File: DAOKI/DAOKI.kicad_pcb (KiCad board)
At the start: 2 copper layers, 34 x 14 mm, 15 parts, among them CON4 CON4, U1 MOCH22a1, U2 LM393

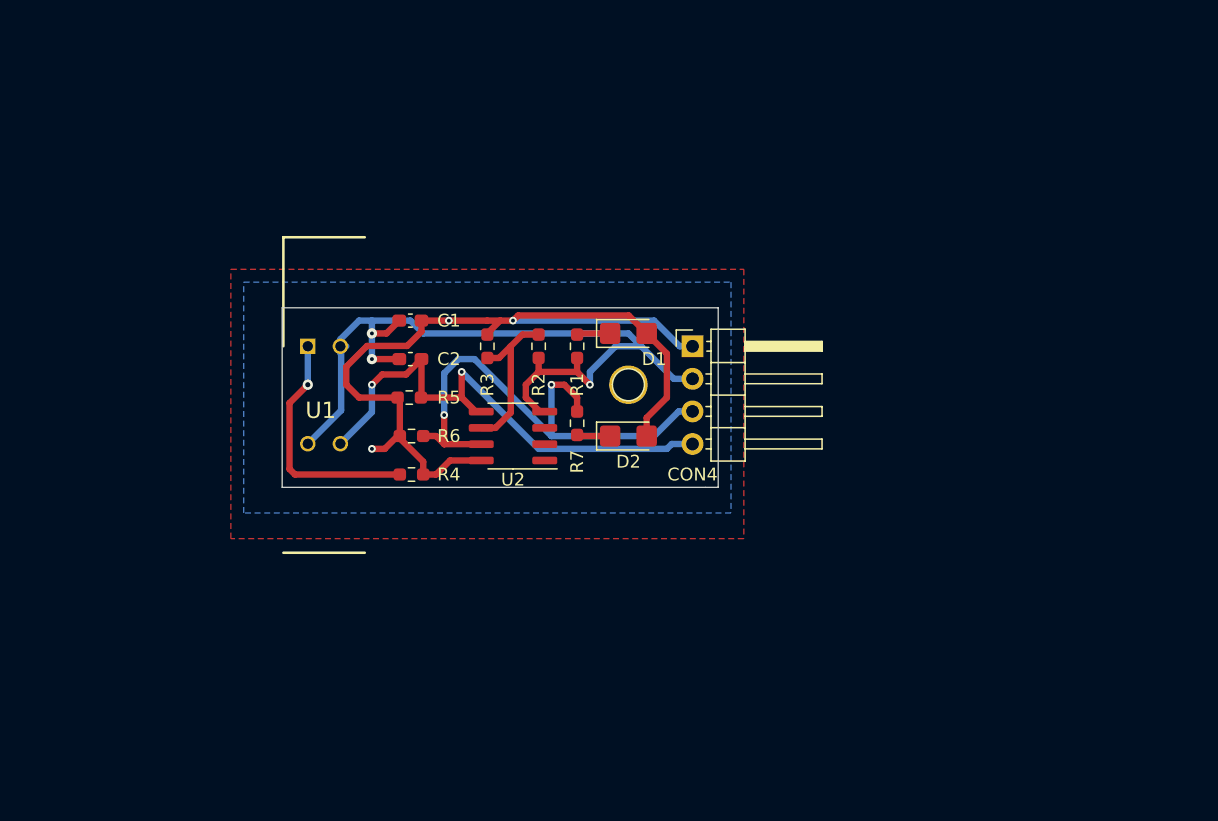
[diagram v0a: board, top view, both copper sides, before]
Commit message: Some schematic improvements
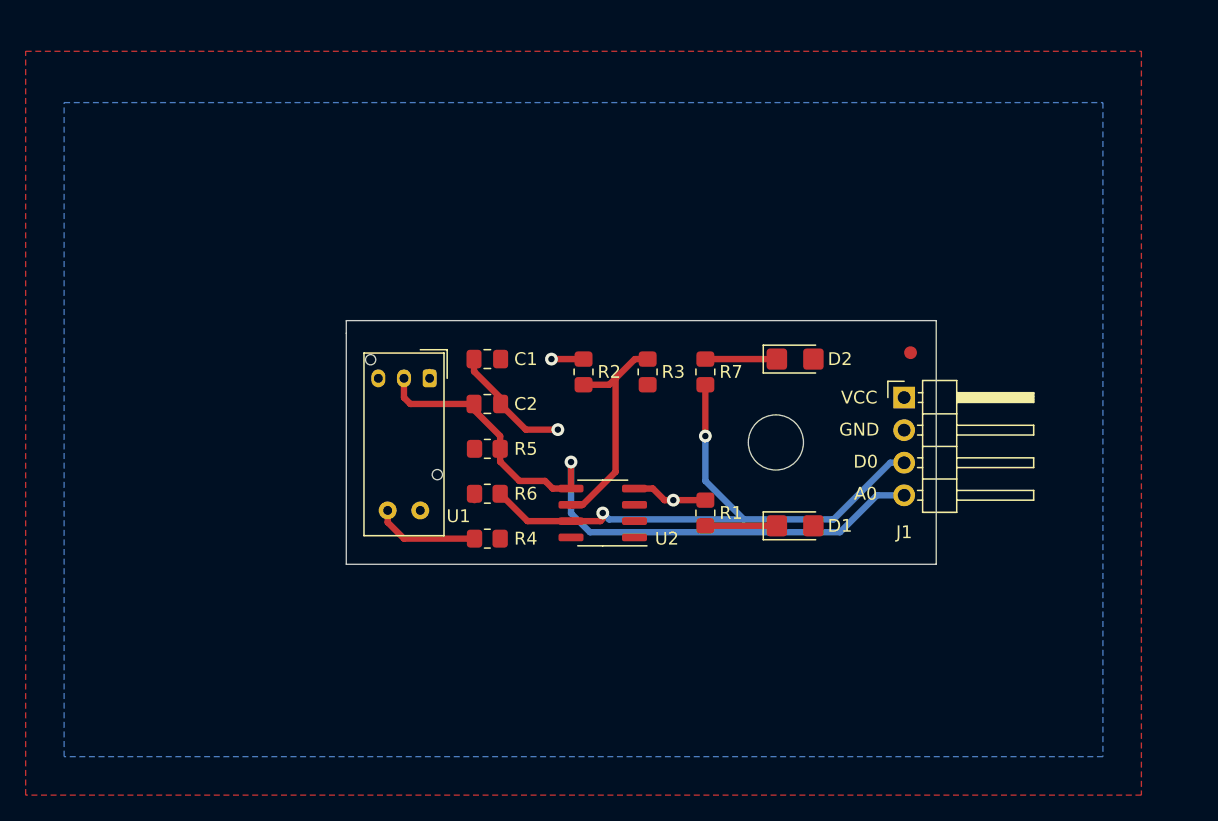
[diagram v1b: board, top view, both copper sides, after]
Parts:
- removed CON4: CON4, Connector_PinHeader_2.54mm:PinHeader_1x04_P2.54mm_Horizontal
- removed REF**: Pin_D1.0mm_L10.0mm, Connector_Pin:Pin_D1.0mm_L10.0mm
- added FID1: Fiducial, Fiducial:Fiducial_1mm_Mask2mm, F.Cu at (172.0, 91.5)
- added H1: Mounting Hole, MountingHole:MountingHole_4.3mm_M4, F.Cu at (161.5, 98.5)
- added J1: CON1, Connector_PinHeader_2.54mm:PinHeader_1x04_P2.54mm_Horizontal, F.Cu at (171.5, 95.0)
- C1, C2: footprint Capacitor_SMD:C_0603_1608Metric_Pad1.08x0.95mm_HandSolder -> Capacitor_SMD:C_0805_2012Metric_Pad1.18x1.45mm_HandSolder
- D1: value POWER INDICATION -> LED POWER
- D2: value SWITCH INDICATION -> LED SWITCH
- R1, R2, R3, R4, R5, R6, R7: footprint Resistor_SMD:R_0603_1608Metric_Pad0.98x0.95mm_HandSolder -> Resistor_SMD:R_0805_2012Metric_Pad1.20x1.40mm_HandSolder
- U1: value MOCH22a1 -> LG206D; footprint DAOKI:DIPS254W40P760L2450H1110Q4N -> OptoDevice:Kodenshi_LG206D
- moved D1 19.8 mm to (163.0, 105.0)
- moved R1 16.4 mm to (156.0, 104.0), turned to 90 degrees
- moved D2 14.3 mm to (163.0, 92.0)
- moved R3 12.7 mm to (151.5, 93.0), turned to 90 degrees
- moved R7 10.8 mm to (156.0, 93.0), turned to 270 degrees
- moved U1 9.82 mm to (134.5, 93.5), turned to 270 degrees
- moved U2 9.22 mm to (148.0, 104.0)
- moved R4 7.74 mm to (139.0, 106.0)
- moved R6 7.43 mm to (139.0, 102.5)
- moved R5 7.28 mm to (139.0, 99.0)
- moved C2 6.95 mm to (139.0, 95.5), turned to 0 degrees
- moved C1 6.71 mm to (139.0, 92.0)
- moved R2 4.03 mm to (146.5, 93.0), turned to 90 degrees
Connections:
- U1 pad 1: Net-(R4-Pad2) -> +5V
- U1 pad 2: GND -> Net-(C2-Pad1)
- U1 pad 3: Net-(C2-Pad1) -> GND
- U1 pad 4: GND -> Net-(R4-Pad2)
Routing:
- net +5V: track 72.0 -> 1.13 mm, vias 3 -> 0
- net GND: track 64.6 -> 18.1 mm
- net Net-(C2-Pad1): track 40.6 -> 52.8 mm, vias 2 -> 1
- net Net-(R4-Pad2): track 19.1 -> 8.23 mm, vias 1 -> 0
- net Net-(J1-Pad3): track 40.9 -> 47.7 mm
- net Net-(R2-Pad1): track 12.7 -> 17.7 mm
- net Net-(D2-Pad1): track 2.61 -> 5.57 mm
- net Net-(D1-Pad1): track 2.61 -> 5.57 mm
- added copper zone on F.Cu, net +5V
- added copper zone on B.Cu, net GND
- removed copper zone on B.Cu, net +5V
- removed copper zone on F.Cu, net GND
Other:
- board size 34 x 14 mm -> 46 x 19 mm
- net class Default: clearance 0.3 -> 0.45
- rule trace_clearance: 0.3 -> 0.45
- board text added: "A0"
- board text added: "D0"
- board text added: "GND"
- board text added: "VCC"

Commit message: Some fixies on PCB file
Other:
- board text added: "Tacómetro con optoacoplador CESE 2020"
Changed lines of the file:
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@@
   (general
     (thickness 1.6)
-    (drawings 11)
+    (drawings 12)
     (tracks 62)
     (zones 0)
@@
   )
   (page A4)
+  (title_block
+    (title "Réplica de tacómetro por optointerruptor de ranura")
+    (date 2020-11-16)
+    (rev 1.0)
+    (company "Gustavo Ramoscelli - UNS")
+    (comment 1 "Revisor: Diego Brengi")
+    (comment 2 "All rights reserved")
+    (comment 3 "Copyright (c) 2020, Gustavo Ramoscelli")
+    (comment 4 "BSD Clausule-3 License")
+  )
   (layers
-    (0 F.Cu signal)
-    (31 B.Cu signal)
+    (0 F.Cu signal hide)
+    (31 B.Cu signal hide)
     (32 B.Adhes user)
     (33 F.Adhes user)
@@
     (mod_text_size 1 1)
     (mod_text_width 0.15)
-    (pad_size 1.524 1.524)
-    (pad_drill 0.762)
+    (pad_size 3.5 3.5)
+    (pad_drill 3.5)
     (pad_to_mask_clearance 0)
     (aux_axis_origin 0 0)
@@
       (effects (font (size 1 1) (thickness 0.15)))
     )
-    (pad 1 np_thru_hole circle (at 0 0) (size 4.3 4.3) (drill 4.3) (layers *.Cu *.Mask))
+    (pad "" np_thru_hole circle (at 0 0) (size 3.5 3.5) (drill 3.5) (layers *.Cu *.Mask))
   )
   (module Fiducial:Fiducial_1mm_Mask2mm (layer F.Cu)
@@
     )
   )
+  (gr_text "Tacómetro con\noptoacoplador\nCESE 2020" (at 144 98) (layer F.SilkS)
+    (effects (font (size 1 1) (thickness 0.15)) (justify left))
+  )
   (dimension 19 (width 0.15) (layer Dwgs.User)
-    (gr_text "19,000 mm" (at 121.7 98.5 270) (layer Dwgs.User)
-      (effects (font (size 1 1) (thickness 0.15)))
-    )
-    (feature1 (pts (xy 128 108) (xy 122.413579 108)))
-    (feature2 (pts (xy 128 89) (xy 122.413579 89)))
-    (crossbar (pts (xy 123 89) (xy 123 108)))
-    (arrow1a (pts (xy 123 108) (xy 122.413579 106.873496)))
-    (arrow1b (pts (xy 123 108) (xy 123.586421 106.873496)))
-    (arrow2a (pts (xy 123 89) (xy 122.413579 90.126504)))
-    (arrow2b (pts (xy 123 89) (xy 123.586421 90.126504)))
+    (gr_text "19,000 mm" (at 185.3 98.5 90) (layer Dwgs.User)
+      (effects (font (size 1 1) (thickness 0.15)))
+    )
+    (feature1 (pts (xy 174 89) (xy 184.586421 89)))
+    (feature2 (pts (xy 174 108) (xy 184.586421 108)))
+    (crossbar (pts (xy 184 108) (xy 184 89)))
+    (arrow1a (pts (xy 184 89) (xy 184.586421 90.126504)))
+    (arrow1b (pts (xy 184 89) (xy 183.413579 90.126504)))
+    (arrow2a (pts (xy 184 108) (xy 184.586421 106.873496)))
+    (arrow2b (pts (xy 184 108) (xy 183.413579 106.873496)))
   )
   (dimension 46 (width 0.15) (layer Dwgs.User)

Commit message: add PCB notes
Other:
- rule trace_min: 0.2 -> 0.5
- rule via_min_size: 0.4 -> 1
- board text added: "Grilla de posicionamiento 1mm Grilla de ruteo 0,5mm Ancho de pista 0,5 mm Diámetro de agujero 0,5 mm Diámetro de pad o vía 1,0 mm Separación entre pistas 0,45 mm Separación entre pista y pad/vía 0,45 mm Separación entre cobre y borde de la placa 0,5 mm Separación entre componentes 0,45 (excepto U1)"
- board text added: "Se uso la información técnica de Mayer SA http://www.mayerpcb.com/informacion-tecnica.html"

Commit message: final fixies on notes to PCB maker
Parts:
- moved C1 4.47 mm to (143.0, 90.0)
- moved C2 4.47 mm to (143.0, 93.5)
- moved D1 4.47 mm to (167.0, 103.0)
- moved D2 4.47 mm to (167.0, 90.0)
- moved FID1 4.47 mm to (176.0, 89.5)
- moved H1 4.47 mm to (165.5, 96.5)
- moved J1 4.47 mm to (175.5, 93.0)
- moved R1 4.47 mm to (160.0, 102.0)
- moved R2 4.47 mm to (150.5, 91.0)
- moved R3 4.47 mm to (155.5, 91.0)
- moved R4 4.47 mm to (143.0, 104.0)
- moved R5 4.47 mm to (143.0, 97.0)
- moved R6 4.47 mm to (143.0, 100.5)
- moved R7 4.47 mm to (160.0, 91.0)
- moved U1 4.47 mm to (138.5, 91.5)
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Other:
- board text added: "Grilla de posicionamiento 1mm Grilla de ruteo 0,5mm Ancho de pista 0,5 mm Diámetro de agujero 0,5 mm Diámetro de pad o vía 1,0 mm Separación entre pistas 0,45 mm Separación entre pista y pad/vía 0,45 mm Separación entre cobre y borde de la placa 0,5 mm Separación entre componentes 0,45 Recubrimiento de pads: Cu + Flux Terminaciones de Pads: HASL Material PCB: FR4 PCB doble faz"
- board text removed: "Grilla de posicionamiento 1mm Grilla de ruteo 0,5mm Ancho de pista 0,5 mm Diámetro de agujero 0,5 mm Diámetro de pad o vía 1,0 mm Separación entre pistas 0,45 mm Separación entre pista y pad/vía 0,45 mm Separación entre cobre y borde de la placa 0,5 mm Separación entre componentes 0,45 (excepto U1)"
